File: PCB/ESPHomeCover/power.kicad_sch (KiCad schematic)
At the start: 4 parts, among them X1 24V

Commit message: Add Board
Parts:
- removed JP1: ~, symbol Jumper:Jumper_2_Open
- removed TP1: 3V3, symbol Connector:TestPoint
- removed U1: ~, Own_Lib:LM2596S Modul, symbol own lib:LM2596S Modul
- added C13: 100nF 35V, Capacitor_SMD:C_0603_1608Metric, symbol Device:C
- added C14: 10uF 35V, Capacitor_SMD:C_0805_2012Metric, symbol Device:C
- added C15: 100nF 6.3V, Capacitor_SMD:C_0805_2012Metric, symbol Device:C
- added C16, C17: 22uF 6.3V, Capacitor_SMD:C_0805_2012Metric, symbol Device:C
- added C18, C19: 100uF 35V, Capacitor_SMD:CP_Elec_6.3x7.7, symbol Device:C_Polarized
- added L1: 4.7uH, Inductor_SMD:L_1812_4532Metric, symbol Device:L
- added TP1: +24V, TestPoint:TestPoint_Pad_2.0x2.0mm, symbol Connector:TestPoint_Alt
- added TP2: +3V3, TestPoint:TestPoint_Pad_2.0x2.0mm, symbol Connector:TestPoint_Alt
- added TP3: GND, TestPoint:TestPoint_Pad_2.0x2.0mm, symbol Connector:TestPoint_Alt
- added U3: AP63203WU-7, Package_TO_SOT_SMD:TSOT-23-6, symbol SamacSys_Parts:AP63203WU-7
- J1: renamed from X1; footprint (none) -> Connector_JST:JST_XH_B2B-XH-A_1x02_P2.50mm_Vertical
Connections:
- net +24V: now also C13.1, C14.1, C18.1, C19.1, TP1.1, U3.2 (EN), U3.3 (VIN)
- net +3V3: now also C16.1, C17.1, L1.2, TP2.1, U3.1 (FB)
- net GND: now also C13.2, C14.2, C16.2, C17.2, C18.2, C19.2, TP3.1, U3.4 (GND)
- new net: C15.1, U3.6 (BST)
- new net: C15.2, L1.1, U3.5 (SW)
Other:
- note added: "Test points"

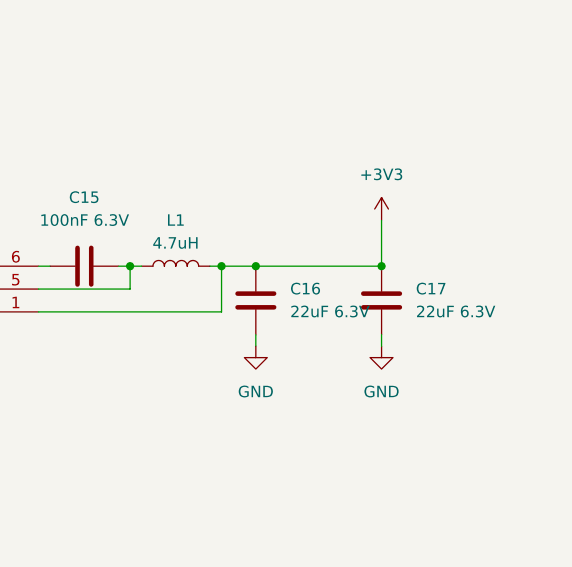
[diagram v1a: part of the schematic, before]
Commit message: small changes
change all Caps to 0603,
add bom
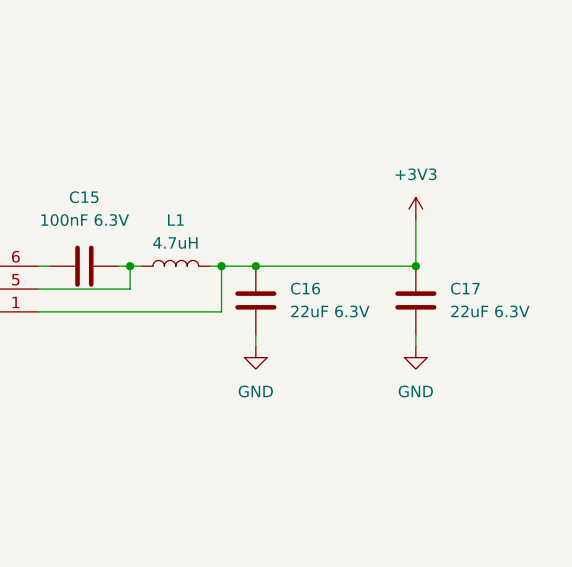
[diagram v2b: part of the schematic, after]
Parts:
- C14: footprint Capacitor_SMD:C_0805_2012Metric -> Capacitor_SMD:C_0603_1608Metric; LCSC C162422 -> C194427
- C15: footprint Capacitor_SMD:C_0805_2012Metric -> Capacitor_SMD:C_0603_1608Metric; LCSC C1854118 -> (none)
- C16, C17: footprint Capacitor_SMD:C_0805_2012Metric -> Capacitor_SMD:C_0603_1608Metric; LCSC C77071 -> C159801
- TP1, TP2, TP3: footprint TestPoint:TestPoint_Pad_2.0x2.0mm -> TestPoint:TestPoint_Pad_1.0x1.0mm
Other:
- company: (none) -> Tim
- moved on the sheet: C17
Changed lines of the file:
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@@
 	(title_block
 		(title "ESPHome Cover PCB")
-		(date "2024-05-08")
-		(rev "1")
+		(date "2024-05-12")
+		(rev "2")
+		(company "Tim")
+	)
+	(junction
+		(at 201.93 86.36)
+		(diameter 0)
+		(color 0 0 0 0)
 	)
 	(junction
@@
 	)
 	(junction
-		(at 198.12 86.36)
-		(diameter 0)
-		(color 0 0 0 0)
-	)
-	(junction
 		(at 102.87 86.36)
 		(diameter 0)
@@
 	(wire
 		(pts
-			(xy 198.12 81.28) (xy 198.12 86.36)
+			(xy 201.93 81.28) (xy 201.93 86.36)
 		)
 		(stroke
@@
 	(wire
 		(pts
-			(xy 198.12 93.98) (xy 198.12 95.25)
+			(xy 201.93 93.98) (xy 201.93 95.25)
 		)
 		(stroke
@@
 	(wire
 		(pts
-			(xy 198.12 86.36) (xy 184.15 86.36)
+			(xy 184.15 86.36) (xy 201.93 86.36)
 		)
 		(stroke
@@
 		(property "LCSC" "C72478"
 			(at 36.83 146.05 90)
+			(effects
+				(font
+					(size 1.27 1.27)
+				)
+				(hide yes)
+			)
+		)
+		(property "Mouser" ""
+			(at 36.83 146.05 0)
 			(effects
 				(font
@@
 			)
 		)
-		(property "Footprint" "Capacitor_SMD:C_0805_2012Metric"
+		(property "Footprint" "Capacitor_SMD:C_0603_1608Metric"
 			(at 168.91 85.3948 0)
 			(effects
@@
 			)
 		)
-		(property "LCSC" "C1854118"
+		(property "LCSC" ""
+			(at 165.1 86.36 0)
+			(effects
+				(font
+					(size 1.27 1.27)
+				)
+				(hide yes)
+			)
+		)
+		(property "Mouser" ""
 			(at 165.1 86.36 0)
 			(effects
@@
 			)
 		)
-		(property "Footprint" "Capacitor_SMD:C_0805_2012Metric"
+		(property "Footprint" "Capacitor_SMD:C_0603_1608Metric"
 			(at 103.8352 93.98 0)
 			(effects
@@
 			)
 		)
-		(property "LCSC" "C162422"
+		(property "LCSC" "C194427"
+			(at 102.87 90.17 0)
+			(effects
+				(font
+					(size 1.27 1.27)
+				)
+				(hide yes)
+			)
+		)
+		(property "Mouser" ""
 			(at 102.87 90.17 0)
 			(effects
@@
 			)
 		)
-		(property "Footprint" "TestPoint:TestPoint_Pad_2.0x2.0mm"
+		(property "Footprint" "TestPoint:TestPoint_Pad_1.0x1.0mm"
 			(at 144.78 179.07 0)
 			(effects
@@
 		)
 		(property "Description" "test point (alternative shape)"
+			(at 144.78 184.15 0)
+			(effects
+				(font
+					(size 1.27 1.27)
+				)
+				(hide yes)
+			)
+		)
+		(property "Mouser" ""
 			(at 144.78 184.15 0)
 			(effects
@@
 	(symbol
 		(lib_id "power:GND")
-		(at 198.12 95.25 0)
+		(at 201.93 95.25 0)
 		(unit 1)
 		(exclude_from_sim no)
@@
 		(fields_autoplaced yes)
 		(property "Reference" "#PWR044"
-			(at 198.12 101.6 0)
+			(at 201.93 101.6 0)
 			(effects
 				(font
@@
 		)
 		(property "Value" "GND"
-			(at 198.12 100.33 0)
+			(at 201.93 100.33 0)
 			(effects
 				(font
@@
 		)
 		(property "Footprint" ""
-			(at 198.12 95.25 0)
+			(at 201.93 95.25 0)
 			(effects
 				(font
@@
 		)
 		(property "Datasheet" ""
-			(at 198.12 95.25 0)
+			(at 201.93 95.25 0)
 			(effects
 				(font
@@
 		)
 		(property "Description" "Power symbol creates a global label with name \"GND\" , ground"
-			(at 198.12 95.25 0)
+			(at 201.93 95.25 0)
 			(effects
 				(font
@@
 			)
 		)
+		(property "Mouser" ""
+			(at 175.26 86.36 0)
+			(effects
+				(font
+					(size 1.27 1.27)
+				)
+				(hide yes)
+			)
+		)
 		(pin "1"
 		)
@@
 			)
 		)
-		(property "Footprint" "TestPoint:TestPoint_Pad_2.0x2.0mm"
+		(property "Footprint" "TestPoint:TestPoint_Pad_1.0x1.0mm"
 			(at 144.78 171.45 0)
 			(effects
@@
 		)
 		(property "Description" "test point (alternative shape)"
+			(at 144.78 176.53 0)
+			(effects
+				(font
+					(size 1.27 1.27)
+				)
+				(hide yes)
+			)
+		)
+		(property "Mouser" ""
 			(at 144.78 176.53 0)
 			(effects
@@
 			)
 		)
-		(property "Footprint" "Capacitor_SMD:C_0805_2012Metric"
+		(property "Footprint" "Capacitor_SMD:C_0603_1608Metric"
 			(at 185.1152 93.98 0)
 			(effects
@@
 			)
 		)
-		(property "LCSC" "C77071"
+		(property "LCSC" "C159801"
+			(at 184.15 90.17 0)
+			(effects
+				(font
+					(size 1.27 1.27)
+				)
+				(hide yes)
+			)
+		)
+		(property "Mouser" ""
 			(at 184.15 90.17 0)
 			(effects
@@
 			)
 		)
+		(property "Mouser" ""
+			(at 134.62 86.36 0)
+			(effects
+				(font
+					(size 1.27 1.27)
+				)
+				(hide yes)
+			)
+		)
 		(pin "4"
 		)
@@
 	(symbol
 		(lib_id "Device:C")
-		(at 198.12 90.17 0)
+		(at 201.93 90.17 0)
 		(unit 1)
 		(exclude_from_sim no)
@@
 		(fields_autoplaced yes)
 		(property "Reference" "C17"
-			(at 201.93 88.8999 0)
+			(at 205.74 88.8999 0)
 			(effects
 				(font
@@
 		)
 		(property "Value" "22uF 6.3V"
-			(at 201.93 91.4399 0)
+			(at 205.74 91.4399 0)
 			(effects
 				(font
@@
 			)
 		)
-		(property "Footprint" "Capacitor_SMD:C_0805_2012Metric"
-			(at 199.0852 93.98 0)
+		(property "Footprint" "Capacitor_SMD:C_0603_1608Metric"
+			(at 202.8952 93.98 0)
 			(effects
 				(font
@@
 		)
 		(property "Datasheet" "~"
-			(at 198.12 90.17 0)
+			(at 201.93 90.17 0)
 			(effects
 				(font
@@
 		)
 		(property "Description" "Unpolarized capacitor"
-			(at 198.12 90.17 0)
-			(effects
-				(font
-					(size 1.27 1.27)
-				)
-				(hide yes)
-			)
-		)
-		(property "LCSC" "C77071"
-			(at 198.12 90.17 0)
+			(at 201.93 90.17 0)
+			(effects
+				(font
+					(size 1.27 1.27)
+				)
+				(hide yes)
+			)
+		)
+		(property "LCSC" "C159801"
+			(at 201.93 90.17 0)
+			(effects
+				(font
+					(size 1.27 1.27)
+				)
+				(hide yes)
+			)
+		)
+		(property "Mouser" ""
+			(at 201.93 90.17 0)
 			(effects
 				(font
@@
 			)
 		)
+		(property "Mouser" ""
+			(at 118.11 90.17 0)
+			(effects
+				(font
+					(size 1.27 1.27)
+				)
+				(hide yes)
+			)
+		)
 		(pin "2"
 		)
@@
 			)
 		)
+		(property "Mouser" ""
+			(at 36.83 158.75 0)
+			(effects
+				(font
+					(size 1.27 1.27)
+				)
+				(hide yes)
+			)
+		)
 		(pin "1"
 		)
@@
 			)
 		)
-		(property "Footprint" "TestPoint:TestPoint_Pad_2.0x2.0mm"
+		(property "Footprint" "TestPoint:TestPoint_Pad_1.0x1.0mm"
 			(at 144.78 163.83 0)
 			(effects
@@
 		)
 		(property "Description" "test point (alternative shape)"
+			(at 144.78 168.91 0)
+			(effects
+				(font
+					(size 1.27 1.27)
+				)
+				(hide yes)
+			)
+		)
+		(property "Mouser" ""
 			(at 144.78 168.91 0)
 			(effects
@@
 			)
 		)
+		(property "Mouser" ""
+			(at 24.13 181.61 0)
+			(effects
+				(font
+					(size 1.27 1.27)
+				)
+				(hide yes)
+			)
+		)
 		(pin "2"
 		)
@@
 	(symbol
 		(lib_id "power:+3V3")
-		(at 198.12 81.28 0)
+		(at 201.93 81.28 0)
 		(unit 1)
 		(exclude_from_sim no)
@@
 		(fields_autoplaced yes)
 		(property "Reference" "#PWR040"
-			(at 198.12 85.09 0)
+			(at 201.93 85.09 0)
 			(effects
 				(font
@@
 		)
 		(property "Value" "+3V3"
-			(at 198.12 76.2 0)
+			(at 201.93 76.2 0)
 			(effects
 				(font
@@
 		)
 		(property "Footprint" ""
-			(at 198.12 81.28 0)
+			(at 201.93 81.28 0)
 			(effects
 				(font
@@
 		)
 		(property "Datasheet" ""
-			(at 198.12 81.28 0)
+			(at 201.93 81.28 0)
 			(effects
 				(font
@@
 		)
 		(property "Description" "Power symbol creates a global label with name \"+3V3\""
-			(at 198.12 81.28 0)
-			(effects
-				(font
+			(at 201.93 81.28 0)
+			(effects
+				(font

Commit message: update PCB
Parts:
- added JP3: ~, Jumper:SolderJumper-2_P1.3mm_Open_RoundedPad1.0x1.5mm, symbol Jumper:Jumper_2_Small_Open
- C13: Mouser Part Number (none) -> 963-GMK107B7104KAHT
- C14: Mouser Part Number (none) -> 81-GRM188R6YA106MA3J
- C15: Mouser Part Number (none) -> 581-06036C104JAT2A
- C16, C17: Mouser Part Number (none) -> 963-MSASJ168BB5226MT
- C18, C19: Mouser Part Number (none) -> 667-EEH-ZK1V101XP
- L1: Mouser Part Number (none) -> 871-B82432T1472K
- renumbered J1 to J7, U3 to U2
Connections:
- net +3V3: now also JP3.1 (A), JP3.2 (B)

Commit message: update PCB
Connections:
- net +24V: now also J7.2 (Pin_2); no longer J7.1 (Pin_1)
- net GND: now also J7.1 (Pin_1); no longer J7.2 (Pin_2)
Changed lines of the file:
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@@
+	(wire
+		(pts
+			(xy 29.21 181.61) (xy 36.83 181.61)
+		)
+		(stroke
+			(width 0)
+			(type default)
+		)
+	)
+	(wire
+		(pts
+			(xy 201.93 85.09) (xy 201.93 86.36)
+		)
+		(stroke
+			(width 0)
+			(type default)
+		)
+	)
+	(wire
+		(pts
+			(xy 160.02 86.36) (xy 161.29 86.36)
+		)
+		(stroke
+			(width 0)
+			(type default)
+		)
+	)
+	(wire
+		(pts
+			(xy 160.02 88.9) (xy 170.18 88.9)
+		)
+		(stroke
+			(width 0)
+			(type default)
+		)
+	)
+	(wire
+		(pts
+			(xy 96.52 86.36) (xy 102.87 86.36)
+		)
+		(stroke
+			(width 0)
+			(type default)
+		)
+	)
+	(wire
+		(pts
+			(xy 180.34 91.44) (xy 180.34 86.36)
+		)
+		(stroke
+			(width 0)
+			(type default)
+		)
+	)
+	(wire
+		(pts
+			(xy 184.15 93.98) (xy 184.15 95.25)
+		)
+		(stroke
+			(width 0)
+			(type default)
+		)
+	)
+	(wire
+		(pts
+			(xy 151.13 161.29) (xy 153.67 161.29)
+		)
+		(stroke
+			(width 0)
+			(type default)
+		)
+	)
 	(wire
 		(pts
 			(xy 29.21 184.15) (xy 36.83 184.15)
-		)
-		(stroke
-			(width 0)
-			(type default)
-		)
-	)
-	(wire
-		(pts
-			(xy 201.93 85.09) (xy 201.93 86.36)
-		)
-		(stroke
-			(width 0)
-			(type default)
-		)
-	)
-	(wire
-		(pts
-			(xy 160.02 86.36) (xy 161.29 86.36)
-		)
-		(stroke
-			(width 0)
-			(type default)
-		)
-	)
-	(wire
-		(pts
-			(xy 160.02 88.9) (xy 170.18 88.9)
-		)
-		(stroke
-			(width 0)
-			(type default)
-		)
-	)
-	(wire
-		(pts
-			(xy 96.52 86.36) (xy 102.87 86.36)
-		)
-		(stroke
-			(width 0)
-			(type default)
-		)
-	)
-	(wire
-		(pts
-			(xy 180.34 91.44) (xy 180.34 86.36)
-		)
-		(stroke
-			(width 0)
-			(type default)
-		)
-	)
-	(wire
-		(pts
-			(xy 184.15 93.98) (xy 184.15 95.25)
-		)
-		(stroke
-			(width 0)
-			(type default)
-		)
-	)
-	(wire
-		(pts
-			(xy 151.13 161.29) (xy 153.67 161.29)
-		)
-		(stroke
-			(width 0)
-			(type default)
-		)
-	)
-	(wire
-		(pts
-			(xy 29.21 181.61) (xy 39.37 181.61)
 		)
 		(stroke
@@
 	)
 	(label "+24V"
-		(at 39.37 181.61 180)
+		(at 36.83 184.15 180)
 		(fields_autoplaced yes)
 		(effects
@@
 	(symbol
 		(lib_id "power:GND")
-		(at 36.83 184.15 90)
+		(at 36.83 181.61 90)
 		(unit 1)
 		(exclude_from_sim no)
@@
 		(fields_autoplaced yes)
 		(property "Reference" "#PWR01"
-			(at 43.18 184.15 0)
+			(at 43.18 181.61 0)
 			(effects
 				(font
@@
 		)
 		(property "Value" "GND"
-			(at 40.64 184.1499 90)
+			(at 40.64 181.6099 90)
 			(effects
 				(font
@@
 		)
 		(property "Footprint" ""
-			(at 36.83 184.15 0)
+			(at 36.83 181.61 0)
 			(effects
 				(font
@@
 		)
 		(property "Datasheet" ""
-			(at 36.83 184.15 0)
+			(at 36.83 181.61 0)
 			(effects
 				(font
@@
 		)
 		(property "Description" "Power symbol creates a global label with name \"GND\" , ground"
-			(at 36.83 184.15 0)
-			(effects
-				(font
+			(at 36.83 181.61 0)
+			(effects
+				(font
